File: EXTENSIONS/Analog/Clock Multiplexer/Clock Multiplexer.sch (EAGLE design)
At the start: 6 parts

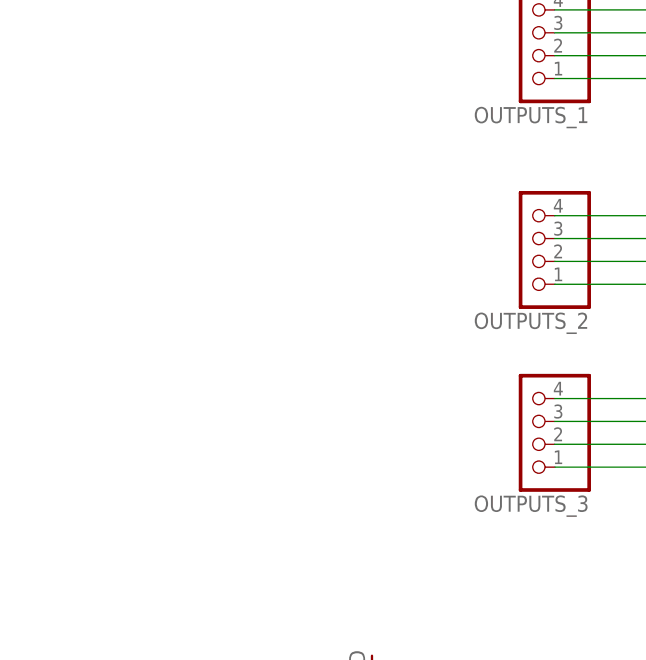
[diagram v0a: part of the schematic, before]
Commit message: Added Clock Multiplexer pcb
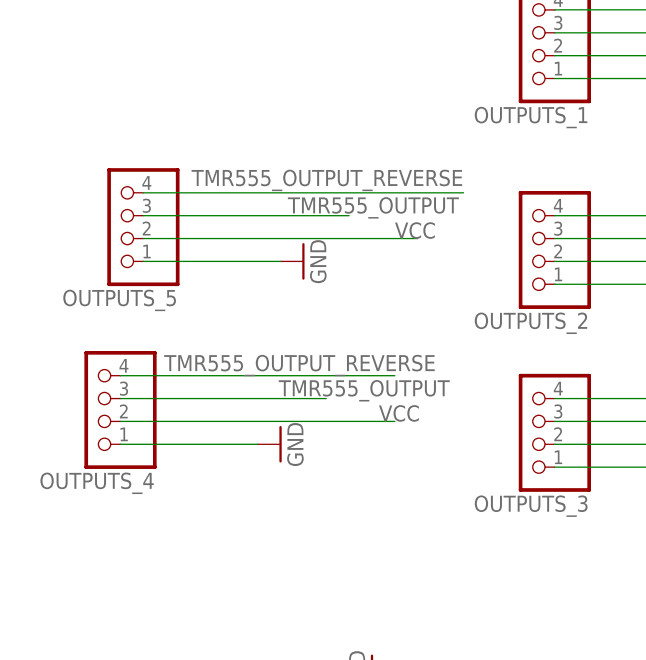
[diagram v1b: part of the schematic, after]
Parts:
- added OUTPUTS_4, OUTPUTS_5: (no value), pinhead:PINHD-1X4
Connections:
- net GND: now also OUTPUTS_4.1, OUTPUTS_5.1
- net TMR555_OUTPUT: now also OUTPUTS_4.3, OUTPUTS_5.3
- net TMR555_OUTPUT_REVERSE: now also OUTPUTS_4.4, OUTPUTS_5.4
- net VCC: now also OUTPUTS_4.2, OUTPUTS_5.2
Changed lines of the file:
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@@
 <part name="GND3" library="supply1" deviceset="GND" device=""/>
 <part name="GND4" library="supply1" deviceset="GND" device=""/>
+<part name="OUTPUTS_4" library="pinhead" deviceset="PINHD-1X4" device=""/>
+<part name="OUTPUTS_5" library="pinhead" deviceset="PINHD-1X4" device=""/>
+<part name="GND6" library="supply1" deviceset="GND" device=""/>
+<part name="GND7" library="supply1" deviceset="GND" device=""/>
 </parts>
 <sheets>
@@
 <instance part="GND3" gate="1" x="71.12" y="76.2" rot="R90"/>
 <instance part="GND4" gate="1" x="71.12" y="55.88" rot="R90"/>
+<instance part="OUTPUTS_4" gate="A" x="-30.48" y="63.5" rot="R180"/>
+<instance part="OUTPUTS_5" gate="A" x="-27.94" y="83.82" rot="R180"/>
+<instance part="GND6" gate="1" x="-7.62" y="78.74" rot="R90"/>
+<instance part="GND7" gate="1" x="-10.16" y="58.42" rot="R90"/>
 </instances>
 <busses>
@@
 <wire x1="20.32" y1="76.2" x2="68.58" y2="76.2" width="0.1524" layer="91"/>
 </segment>
+<segment>
+<pinref part="OUTPUTS_4" gate="A" pin="1"/>
+<pinref part="GND7" gate="1" pin="GND"/>
+<wire x1="-27.94" y1="58.42" x2="-12.7" y2="58.42" width="0.1524" layer="91"/>
+</segment>
+<segment>
+<pinref part="OUTPUTS_5" gate="A" pin="1"/>
+<pinref part="GND6" gate="1" pin="GND"/>
+<wire x1="-25.4" y1="78.74" x2="-10.16" y2="78.74" width="0.1524" layer="91"/>
+</segment>
 </net>
 <net name="VCC" class="0">
@@
 <label x="35.56" y="78.74" size="1.778" layer="95"/>
 </segment>
+<segment>
+<pinref part="OUTPUTS_5" gate="A" pin="2"/>
+<wire x1="-25.4" y1="81.28" x2="5.08" y2="81.28" width="0.1524" layer="91"/>
+<label x="7.112" y="83.058" size="1.778" layer="95" rot="R180"/>
+</segment>
+<segment>
+<pinref part="OUTPUTS_4" gate="A" pin="2"/>
+<wire x1="-27.94" y1="60.96" x2="2.54" y2="60.96" width="0.1524" layer="91"/>
+<label x="5.334" y="62.738" size="1.778" layer="95" rot="R180"/>
+</segment>
 </net>
 <net name="TMR555_OUTPUT" class="0">
@@
 <wire x1="20.32" y1="60.96" x2="48.26" y2="60.96" width="0.1524" layer="91"/>
 <label x="43.18" y="60.96" size="1.778" layer="95"/>
+</segment>
+<segment>
+<pinref part="OUTPUTS_5" gate="A" pin="3"/>
+<wire x1="-25.4" y1="83.82" x2="-2.54" y2="83.82" width="0.1524" layer="91"/>
+<label x="9.652" y="85.852" size="1.778" layer="95" rot="R180"/>
+</segment>
+<segment>
+<pinref part="OUTPUTS_4" gate="A" pin="3"/>
+<wire x1="-27.94" y1="63.5" x2="-5.08" y2="63.5" width="0.1524" layer="91"/>
+<label x="8.636" y="65.532" size="1.778" layer="95" rot="R180"/>
 </segment>
 </net>
@@
 <label x="35.56" y="63.5" size="1.778" layer="95"/>
 </segment>
+<segment>
+<pinref part="OUTPUTS_5" gate="A" pin="4"/>
+<wire x1="-25.4" y1="86.36" x2="10.16" y2="86.36" width="0.1524" layer="91"/>
+<label x="10.16" y="88.9" size="1.778" layer="95" rot="R180"/>
+</segment>
+<segment>
+<pinref part="OUTPUTS_4" gate="A" pin="4"/>
+<wire x1="-27.94" y1="66.04" x2="2.54" y2="66.04" width="0.1524" layer="91"/>
+<label x="7.112" y="68.326" size="1.778" layer="95" rot="R180"/>
+</segment>
 </net>

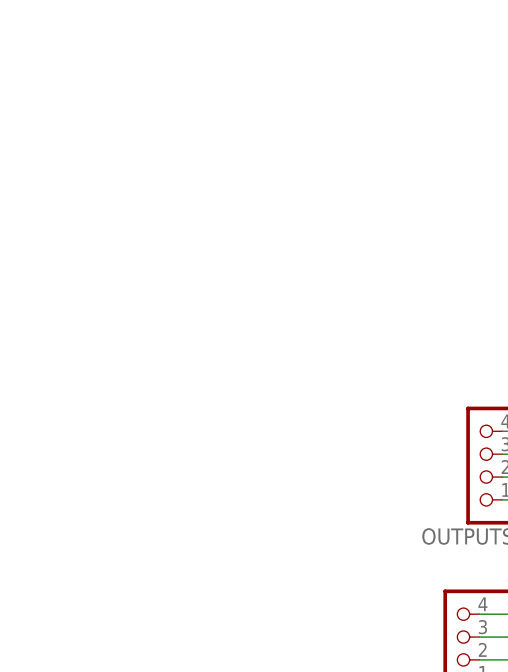
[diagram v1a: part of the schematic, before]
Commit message: Added Clock Multiplexer pcb
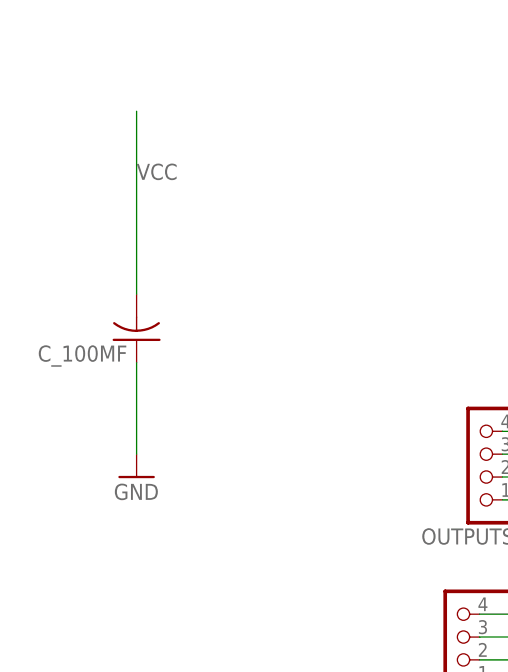
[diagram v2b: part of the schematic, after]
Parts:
- added C_100MF: (no value), adafruit:C-US025-030X050
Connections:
- net GND: now also C_100MF.1
- net VCC: now also C_100MF.2
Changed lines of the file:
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@@
 <part name="GND6" library="supply1" deviceset="GND" device=""/>
 <part name="GND7" library="supply1" deviceset="GND" device=""/>
+<part name="C_100MF" library="adafruit" deviceset="C-US" device="025-030X050"/>
+<part name="GND8" library="supply1" deviceset="GND" device=""/>
 </parts>
 <sheets>
@@
 <instance part="GND6" gate="1" x="-7.62" y="78.74" rot="R90"/>
 <instance part="GND7" gate="1" x="-10.16" y="58.42" rot="R90"/>
+<instance part="C_100MF" gate="G$1" x="-66.04" y="96.52" rot="R180"/>
+<instance part="GND8" gate="1" x="-66.04" y="81.28"/>
 </instances>
 <busses>
@@
 <wire x1="-25.4" y1="78.74" x2="-10.16" y2="78.74" width="0.1524" layer="91"/>
 </segment>
+<segment>
+<pinref part="C_100MF" gate="G$1" pin="1"/>
+<pinref part="GND8" gate="1" pin="GND"/>
+<wire x1="-66.04" y1="93.98" x2="-66.04" y2="83.82" width="0.1524" layer="91"/>
+</segment>
 </net>
 <net name="VCC" class="0">
@@
 <label x="5.334" y="62.738" size="1.778" layer="95" rot="R180"/>
 </segment>
+<segment>
+<pinref part="C_100MF" gate="G$1" pin="2"/>
+<wire x1="-66.04" y1="101.6" x2="-66.04" y2="121.92" width="0.1524" layer="91"/>
+<label x="-66.04" y="114.3" size="1.778" layer="95"/>
+</segment>
 </net>

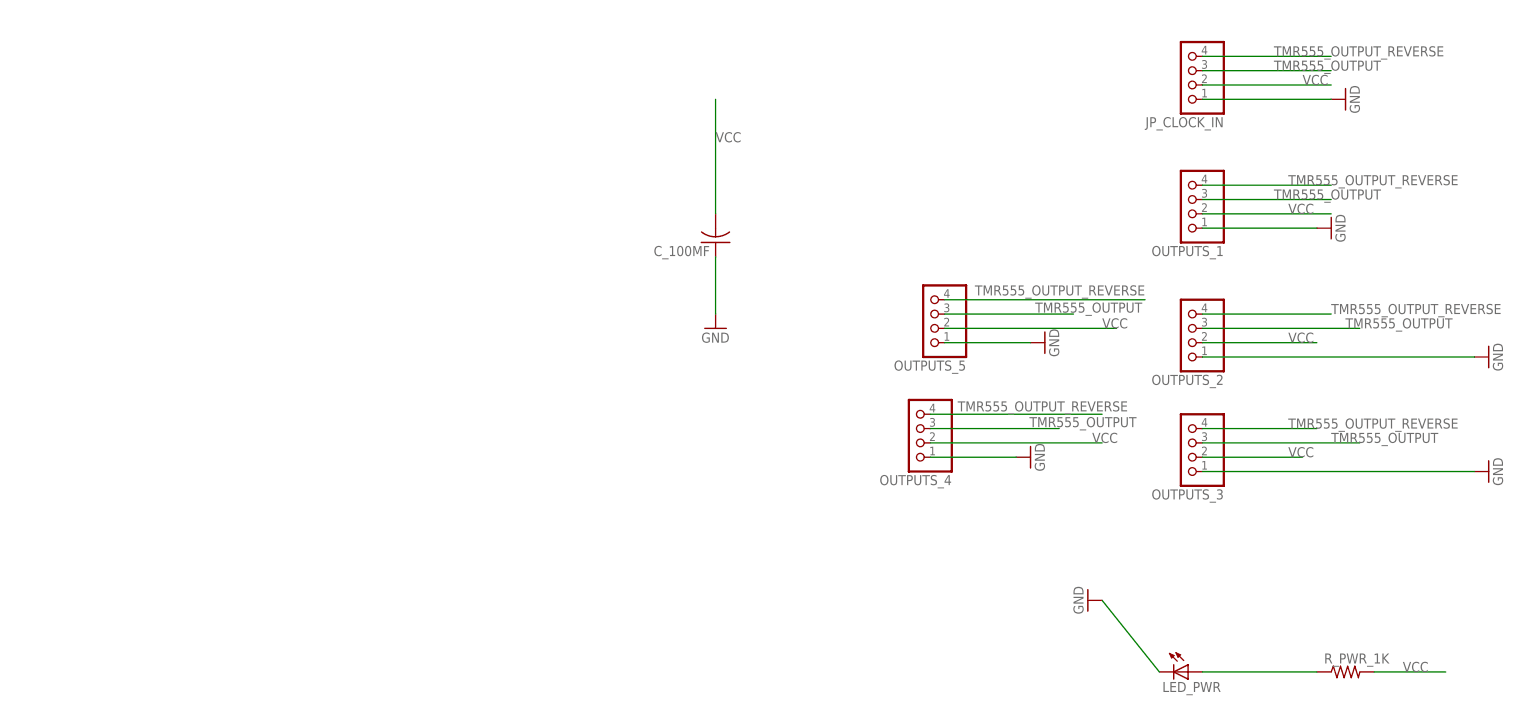
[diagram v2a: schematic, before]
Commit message: update clock multiplexer
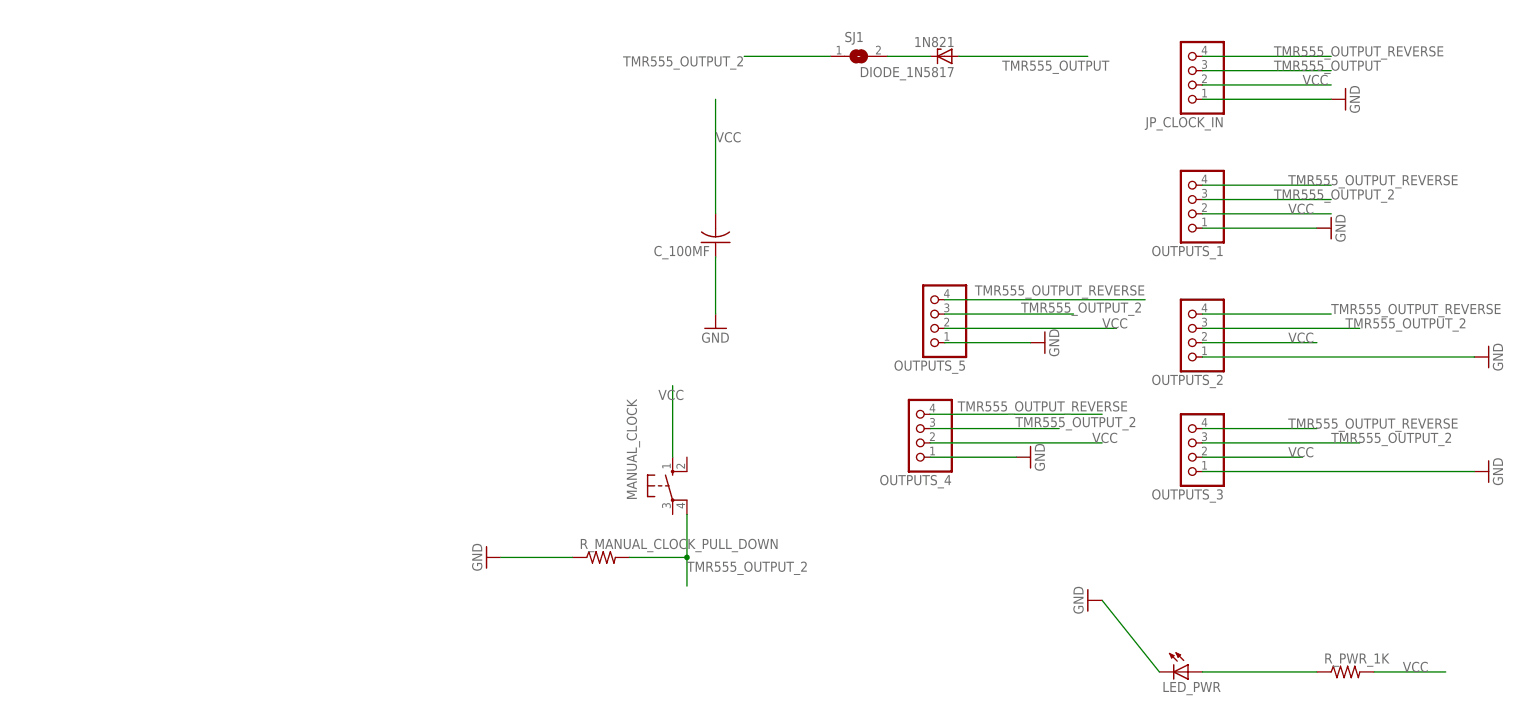
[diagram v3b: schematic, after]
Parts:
- added DIODE_1N5817: 1N821, diode:1N821
- added MANUAL_CLOCK: (no value), switch-omron:10-XX
- added R_MANUAL_CLOCK_PULL_DOWN: (no value), adafruit:R-US_R1206
- added SJ1: (no value), microbuilder:SOLDERJUMPERREFLOW
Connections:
- new net N$2: DIODE_1N5817.C, SJ1.2
- new net TMR555_OUTPUT_2: MANUAL_CLOCK.P1, OUTPUTS_1.3, OUTPUTS_2.3, OUTPUTS_3.3, OUTPUTS_4.3, OUTPUTS_5.3, R_MANUAL_CLOCK_PULL_DOWN.2, SJ1.1
- net GND: now also R_MANUAL_CLOCK_PULL_DOWN.1
- net TMR555_OUTPUT: now also DIODE_1N5817.A; no longer OUTPUTS_1.3, OUTPUTS_2.3, OUTPUTS_3.3, OUTPUTS_4.3, OUTPUTS_5.3
- net VCC: now also MANUAL_CLOCK.S
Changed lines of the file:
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@@
 <part name="C_100MF" library="adafruit" deviceset="C-US" device="025-030X050"/>
 <part name="GND8" library="supply1" deviceset="GND" device=""/>
+<part name="MANUAL_CLOCK" library="switch-omron" deviceset="10-XX" device=""/>
+<part name="R_MANUAL_CLOCK_PULL_DOWN" library="adafruit" deviceset="R-US_" device="R1206"/>
+<part name="GND9" library="supply1" deviceset="GND" device=""/>
+<part name="SJ1" library="microbuilder" deviceset="SOLDERJUMPER" device="REFLOW"/>
+<part name="DIODE_1N5817" library="diode" deviceset="1N821" device=""/>
 </parts>
 <sheets>
@@
 <instance part="C_100MF" gate="G$1" x="-66.04" y="96.52" rot="R180"/>
 <instance part="GND8" gate="1" x="-66.04" y="81.28"/>
+<instance part="MANUAL_CLOCK" gate="1" x="-73.66" y="53.34"/>
+<instance part="R_MANUAL_CLOCK_PULL_DOWN" gate="G$1" x="-86.36" y="40.64"/>
+<instance part="GND9" gate="1" x="-106.68" y="40.64" rot="R270"/>
+<instance part="SJ1" gate="1" x="-40.64" y="129.54"/>
+<instance part="DIODE_1N5817" gate="1" x="-25.4" y="129.54" rot="R180"/>
 </instances>
 <busses>
@@
 <wire x1="-66.04" y1="93.98" x2="-66.04" y2="83.82" width="0.1524" layer="91"/>
 </segment>
+<segment>
+<pinref part="GND9" gate="1" pin="GND"/>
+<pinref part="R_MANUAL_CLOCK_PULL_DOWN" gate="G$1" pin="1"/>
+<wire x1="-104.14" y1="40.64" x2="-91.44" y2="40.64" width="0.1524" layer="91"/>
+</segment>
 </net>
 <net name="VCC" class="0">
@@
 <label x="-66.04" y="114.3" size="1.778" layer="95"/>
 </segment>
+<segment>
+<pinref part="MANUAL_CLOCK" gate="1" pin="S"/>
+<wire x1="-73.66" y1="58.42" x2="-73.66" y2="71.12" width="0.1524" layer="91"/>
+<label x="-76.2" y="68.58" size="1.778" layer="95"/>
+</segment>
 </net>
 <net name="TMR555_OUTPUT" class="0">
@@
 </segment>
 <segment>
+<pinref part="DIODE_1N5817" gate="1" pin="A"/>
+<wire x1="-22.86" y1="129.54" x2="0" y2="129.54" width="0.1524" layer="91"/>
+<label x="3.81" y="128.778" size="1.778" layer="95" rot="R180"/>
+</segment>
+</net>
+<net name="TMR555_OUTPUT_REVERSE" class="0">
+<segment>
+<pinref part="JP_CLOCK_IN" gate="A" pin="4"/>
+<wire x1="20.32" y1="129.54" x2="43.18" y2="129.54" width="0.1524" layer="91"/>
+<label x="33.02" y="129.54" size="1.778" layer="95"/>
+</segment>
+<segment>
+<pinref part="OUTPUTS_1" gate="A" pin="4"/>
+<wire x1="20.32" y1="106.68" x2="43.18" y2="106.68" width="0.1524" layer="91"/>
+<label x="35.56" y="106.68" size="1.778" layer="95"/>
+</segment>
+<segment>
+<pinref part="OUTPUTS_2" gate="A" pin="4"/>
+<wire x1="20.32" y1="83.82" x2="43.18" y2="83.82" width="0.1524" layer="91"/>
+<label x="43.18" y="83.82" size="1.778" layer="95"/>
+</segment>
+<segment>
+<pinref part="OUTPUTS_3" gate="A" pin="4"/>
+<wire x1="20.32" y1="63.5" x2="40.64" y2="63.5" width="0.1524" layer="91"/>
+<label x="35.56" y="63.5" size="1.778" layer="95"/>
+</segment>
+<segment>
+<pinref part="OUTPUTS_5" gate="A" pin="4"/>
+<wire x1="-25.4" y1="86.36" x2="10.16" y2="86.36" width="0.1524" layer="91"/>
+<label x="10.16" y="88.9" size="1.778" layer="95" rot="R180"/>
+</segment>
+<segment>
+<pinref part="OUTPUTS_4" gate="A" pin="4"/>
+<wire x1="-27.94" y1="66.04" x2="2.54" y2="66.04" width="0.1524" layer="91"/>
+<label x="7.112" y="68.326" size="1.778" layer="95" rot="R180"/>
+</segment>
+</net>
+<net name="N$1" class="0">
+<segment>
+<pinref part="R_PWR_1K" gate="G$1" pin="1"/>
+<pinref part="LED_PWR" gate="G$1" pin="A"/>
+<wire x1="40.64" y1="20.32" x2="20.32" y2="20.32" width="0.1524" layer="91"/>
+</segment>
+</net>
+<net name="TMR555_OUTPUT_2" class="0">
+<segment>
 <pinref part="OUTPUTS_1" gate="A" pin="3"/>
 <wire x1="20.32" y1="104.14" x2="43.18" y2="104.14" width="0.1524" layer="91"/>
@@
 </segment>
 <segment>
+<pinref part="OUTPUTS_5" gate="A" pin="3"/>
+<wire x1="-25.4" y1="83.82" x2="-2.54" y2="83.82" width="0.1524" layer="91"/>
+<label x="9.652" y="85.852" size="1.778" layer="95" rot="R180"/>
+</segment>
+<segment>
 <pinref part="OUTPUTS_2" gate="A" pin="3"/>
 <wire x1="20.32" y1="81.28" x2="48.26" y2="81.28" width="0.1524" layer="91"/>
@@
 </segment>
 <segment>
-<pinref part="OUTPUTS_5" gate="A" pin="3"/>
-<wire x1="-25.4" y1="83.82" x2="-2.54" y2="83.82" width="0.1524" layer="91"/>
-<label x="9.652" y="85.852" size="1.778" layer="95" rot="R180"/>
-</segment>
-<segment>
 <pinref part="OUTPUTS_4" gate="A" pin="3"/>
 <wire x1="-27.94" y1="63.5" x2="-5.08" y2="63.5" width="0.1524" layer="91"/>
 <label x="8.636" y="65.532" size="1.778" layer="95" rot="R180"/>
 </segment>
-</net>
-<net name="TMR555_OUTPUT_REVERSE" class="0">
-<segment>
-<pinref part="JP_CLOCK_IN" gate="A" pin="4"/>
-<wire x1="20.32" y1="129.54" x2="43.18" y2="129.54" width="0.1524" layer="91"/>
-<label x="33.02" y="129.54" size="1.778" layer="95"/>
-</segment>
-<segment>
-<pinref part="OUTPUTS_1" gate="A" pin="4"/>
-<wire x1="20.32" y1="106.68" x2="43.18" y2="106.68" width="0.1524" layer="91"/>
-<label x="35.56" y="106.68" size="1.778" layer="95"/>
-</segment>
-<segment>
-<pinref part="OUTPUTS_2" gate="A" pin="4"/>
-<wire x1="20.32" y1="83.82" x2="43.18" y2="83.82" width="0.1524" layer="91"/>
-<label x="43.18" y="83.82" size="1.778" layer="95"/>
-</segment>
-<segment>
-<pinref part="OUTPUTS_3" gate="A" pin="4"/>
-<wire x1="20.32" y1="63.5" x2="40.64" y2="63.5" width="0.1524" layer="91"/>
-<label x="35.56" y="63.5" size="1.778" layer="95"/>
-</segment>
-<segment>
-<pinref part="OUTPUTS_5" gate="A" pin="4"/>
-<wire x1="-25.4" y1="86.36" x2="10.16" y2="86.36" width="0.1524" layer="91"/>
-<label x="10.16" y="88.9" size="1.778" layer="95" rot="R180"/>
-</segment>
-<segment>
-<pinref part="OUTPUTS_4" gate="A" pin="4"/>
-<wire x1="-27.94" y1="66.04" x2="2.54" y2="66.04" width="0.1524" layer="91"/>
-<label x="7.112" y="68.326" size="1.778" layer="95" rot="R180"/>
-</segment>
-</net>
-<net name="N$1" class="0">
-<segment>
-<pinref part="R_PWR_1K" gate="G$1" pin="1"/>
-<pinref part="LED_PWR" gate="G$1" pin="A"/>
-<wire x1="40.64" y1="20.32" x2="20.32" y2="20.32" width="0.1524" layer="91"/>
-</segment>
-</net>
+<segment>
+<pinref part="MANUAL_CLOCK" gate="1" pin="P1"/>
+<wire x1="-71.12" y1="48.26" x2="-71.12" y2="40.64" width="0.1524" layer="91"/>
+<label x="-71.12" y="38.1" size="1.778" layer="95"/>
+<pinref part="R_MANUAL_CLOCK_PULL_DOWN" gate="G$1" pin="2"/>
+<wire x1="-71.12" y1="40.64" x2="-71.12" y2="35.56" width="0.1524" layer="91"/>
+<wire x1="-81.28" y1="40.64" x2="-71.12" y2="40.64" width="0.1524" layer="91"/>
+<junction x="-71.12" y="40.64"/>
+</segment>
+<segment>
+<pinref part="SJ1" gate="1" pin="1"/>
+<wire x1="-45.72" y1="129.54" x2="-60.96" y2="129.54" width="0.1524" layer="91"/>
+<label x="-60.96" y="129.54" size="1.778" layer="95" rot="R180"/>
+</segment>
+</net>
+<net name="N$2" class="0">
+<segment>
+<pinref part="DIODE_1N5817" gate="1" pin="C"/>
+<pinref part="SJ1" gate="1" pin="2"/>
+<wire x1="-27.94" y1="129.54" x2="-35.56" y2="129.54" width="0.1524" layer="91"/>
+</segment>
+</net>
